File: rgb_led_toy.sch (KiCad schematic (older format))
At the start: 53 parts, among them IC1 AT168, IC2 MBI5168, IC3 MBI5168, IC4 MBI5168, P1 I2C, P2 PORTC, P3 FTDI

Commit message: Moved 'led0' to a hardware PWM pin that is actually free to use.
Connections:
- net led0: now also IC1.10 (PD6(AIN0)); no longer IC1.13 (PB1(OC1A))
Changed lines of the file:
@@
-EESchema Schematic File Version 2  date Tue 10 Jan 2012 11:49:42 AM CET
+EESchema Schematic File Version 2  date Wed 11 Jan 2012 03:03:35 PM CET
 LIBS:power
 LIBS:atmega8_168_328_TQFP
@@
 Sheet 1 1
 Title "RGB LED Toy"
-Date "10 jan 2012"
+Date "11 jan 2012"
 Rev "2.0.d"
 Comp "2012 - My 2muF - blog.spitzenpfeil.org"
@@
 Comment4 ""
 $EndDescr
+NoConn ~ 3950 2100
 NoConn ~ 1550 2200
-Wire Wire Line
-	3950 2100 4050 2100
 Connection ~ 3750 5400
 Connection ~ 3350 5400
@@
 Connection ~ 3950 5400
 NoConn ~ 1550 2700
-NoConn ~ 1550 2600
 NoConn ~ 1550 2500
 NoConn ~ 1550 2400
@@
 	1    0    0    -1
 $EndComp
-Text Label 4050 2100 0    60   ~ 0
+Text Label 1550 2600 2    60   ~ 0
 led0
 Text Label 1800 5300 2    60   ~ 0

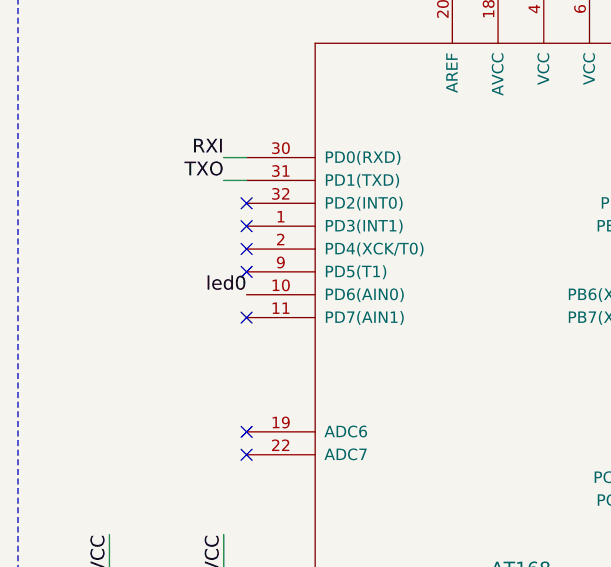
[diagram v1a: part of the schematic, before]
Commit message: Miniscule visual tweak to the schematic.
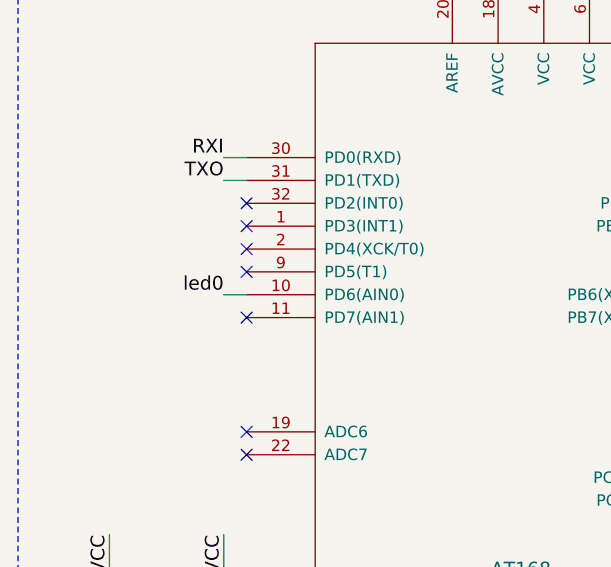
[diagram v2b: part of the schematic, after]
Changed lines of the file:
@@
-EESchema Schematic File Version 2  date Wed 11 Jan 2012 03:03:35 PM CET
+EESchema Schematic File Version 2  date Sat 14 Jan 2012 07:17:03 PM CET
 LIBS:power
 LIBS:atmega8_168_328_TQFP
@@
 Sheet 1 1
 Title "RGB LED Toy"
-Date "11 jan 2012"
+Date "14 jan 2012"
 Rev "2.0.d"
 Comp "2012 - My 2muF - blog.spitzenpfeil.org"
@@
 Comment4 ""
 $EndDescr
-NoConn ~ 3950 2100
-NoConn ~ 1550 2200
 Connection ~ 3750 5400
 Connection ~ 3350 5400
@@
 	2750 5400 4150 5400
 Connection ~ 3950 5400
+Wire Wire Line
+	1450 2600 1550 2600
+NoConn ~ 3950 2100
+NoConn ~ 1550 2200
 NoConn ~ 1550 2700
 NoConn ~ 1550 2500
@@
 	1    0    0    -1
 $EndComp
-Text Label 1550 2600 2    60   ~ 0
+Text Label 1450 2600 2    60   ~ 0
 led0
 Text Label 1800 5300 2    60   ~ 0

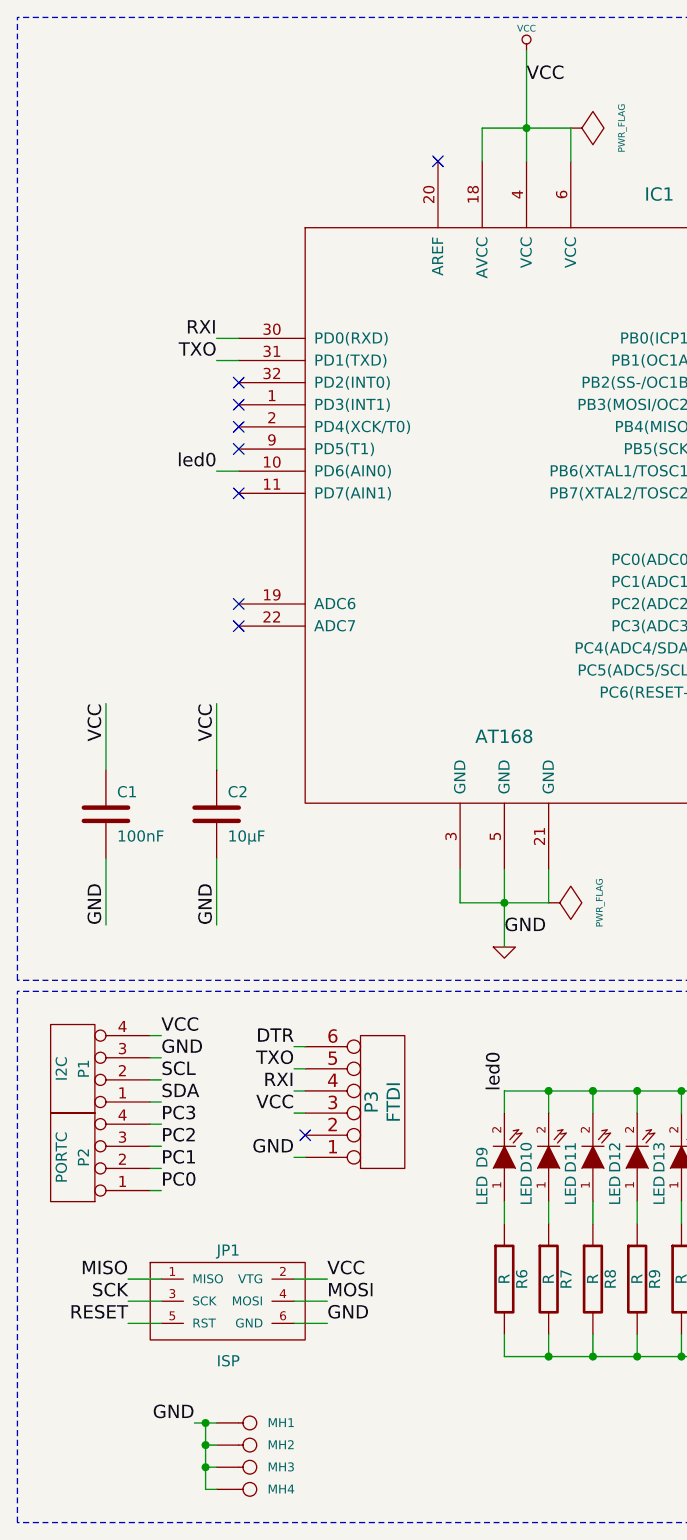
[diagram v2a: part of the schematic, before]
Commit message: Added the TSOP38238 for IR reception to INT0 + some silkscreen art.
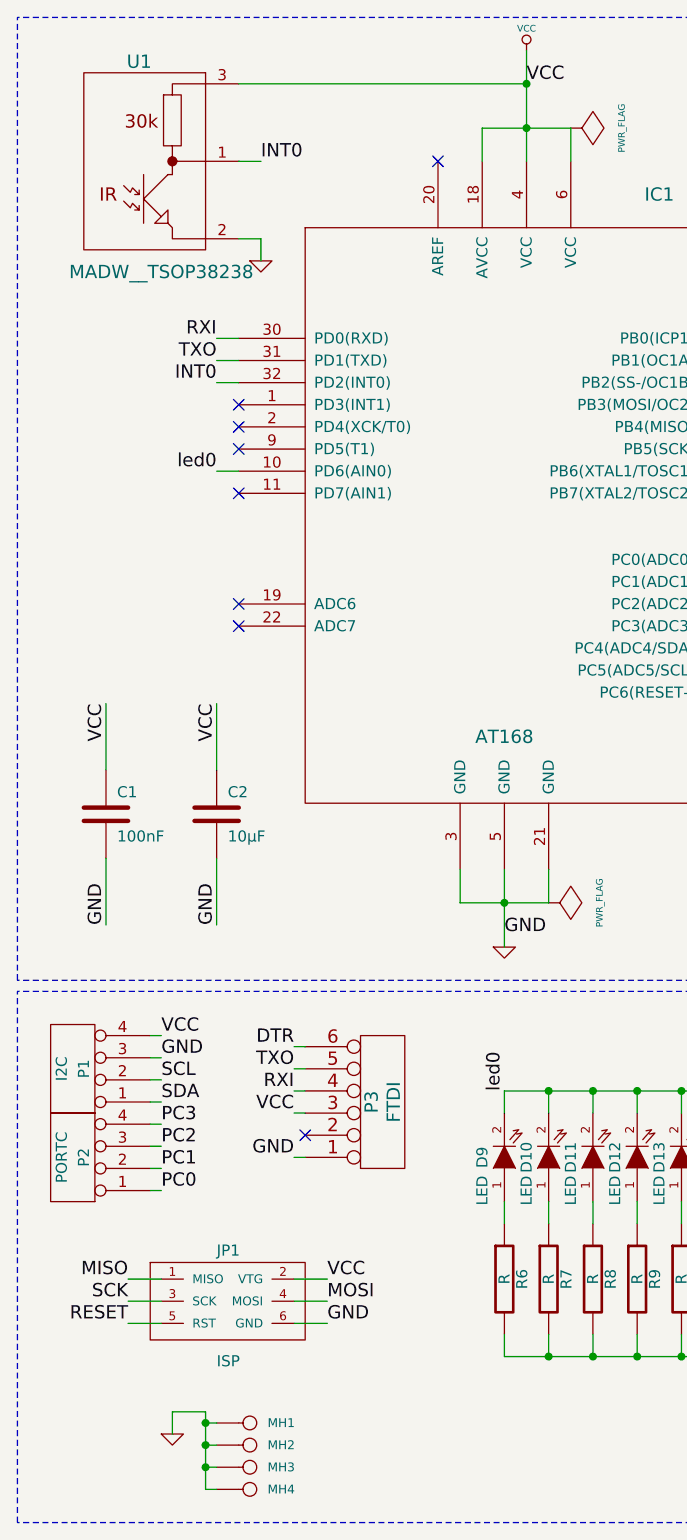
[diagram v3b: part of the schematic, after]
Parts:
- added U1: MADW__TSOP38238, symbol MADW__TSOP38238
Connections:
- net GND: now also U1.2
- net VCC: now also U1.3
- net INT0: now reaches IC1.32 (PD2(INT0))
- net INT0: now also U1.1
- no-connect marks 13 -> 12
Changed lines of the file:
@@
-EESchema Schematic File Version 2  date Sat 14 Jan 2012 07:17:03 PM CET
+EESchema Schematic File Version 2  date Tue 08 May 2012 05:44:56 PM CEST
 LIBS:power
 LIBS:atmega8_168_328_TQFP
@@
 Sheet 1 1
 Title "RGB LED Toy"
-Date "14 jan 2012"
-Rev "2.0.d"
+Date "8 may 2012"
+Rev "2.0.e"
 Comp "2012 - My 2muF - blog.spitzenpfeil.org"
 Comment1 ""
@@
 Comment4 ""
 $EndDescr
+Connection ~ 1400 6900
+Wire Wire Line
+	1250 6950 1250 6850
+Wire Wire Line
+	1250 6850 1400 6850
+Wire Wire Line
+	1400 6850 1400 7200
+Connection ~ 1400 7000
+Wire Wire Line
+	1450 7000 1400 7000
+Wire Wire Line
+	1450 2200 1550 2200
+Connection ~ 2850 850
+Wire Wire Line
+	1550 850  2850 850
 Connection ~ 3750 5400
 Connection ~ 3350 5400
@@
 	1150 5150 1200 5150
 Wire Wire Line
-	1400 7000 1450 7000
-Wire Wire Line
-	1450 7200 1400 7200
-Connection ~ 1400 7000
-Wire Wire Line
 	7250 6550 7300 6550
 Wire Wire Line
@@
 Wire Wire Line
 	6150 6550 6200 6550
-Wire Wire Line
-	1400 7200 1400 6900
-Connection ~ 1400 7100
-Wire Wire Line
-	1400 7100 1450 7100
-Wire Wire Line
-	1450 6900 1350 6900
-Connection ~ 1400 6900
 Wire Wire Line
 	1200 5250 1150 5250
@@
 Wire Wire Line
 	1450 2600 1550 2600
+Wire Wire Line
+	1550 1550 1650 1550
+Wire Wire Line
+	1650 1550 1650 1650
+Wire Wire Line
+	1550 1200 1650 1200
+Wire Wire Line
+	1400 7200 1450 7200
+Wire Wire Line
+	1400 6900 1450 6900
+Wire Wire Line
+	1450 7100 1400 7100
+Connection ~ 1400 7100
+$Comp
+L GND #PWR01
+U 1 1 4FA93F65
+P 1250 6950
+F 0 "#PWR01" H 1250 6950 30  0001 C CNN
+F 1 "GND" H 1250 6880 30  0001 C CNN
+	1    1250 6950
+	1    0    0    -1
+$EndComp
+Text Label 1450 2200 2    60   ~ 0
+INT0
+Text Label 1650 1200 0    60   ~ 0
+INT0
+$Comp
+L GND #PWR02
+U 1 1 4FA92301
+P 1650 1650
+F 0 "#PWR02" H 1650 1650 30  0001 C CNN
+F 1 "GND" H 1650 1580 30  0001 C CNN
+	1    1650 1650
+	1    0    0    -1
+$EndComp
+$Comp
+L MADW__TSOP38238 U1
+U 1 1 4FA922E7
+P 1150 1200
+F 0 "U1" H 1100 1650 60  0000 C CNN
+F 1 "MADW__TSOP38238" H 1200 700 60  0000 C CNN
+	1    1150 1200
+	1    0    0    -1
+$EndComp
 NoConn ~ 3950 2100
-NoConn ~ 1550 2200
 NoConn ~ 1550 2700
 NoConn ~ 1550 2500
@@
 Text Label 6450 4600 2    60   ~ 0
 GND
-Text Label 1350 6900 2    60   ~ 0
-GND
 $Comp
 L CONN_1 MH4
@@
 $EndComp
 $Comp
-L PWR_FLAG #FLG01
+L PWR_FLAG #FLG03
 U 1 1 4EEF9904
 P 2950 4550
-F 0 "#FLG01" H 2950 4820 30  0001 C CNN
+F 0 "#FLG03" H 2950 4820 30  0001 C CNN
 F 1 "PWR_FLAG" H 2950 4780 30  0000 C CNN
 	1    2950 4550
@@
 $EndComp
 $Comp
-L PWR_FLAG #FLG02
+L PWR_FLAG #FLG04
 U 1 1 4EEF98EB
 P 3050 1050
-F 0 "#FLG02" H 3050 1320 30  0001 C CNN
+F 0 "#FLG04" H 3050 1320 30  0001 C CNN
 F 1 "PWR_FLAG" H 3050 1280 30  0000 C CNN
 	1    3050 1050
@@
 GND
 $Comp
-L GND #PWR03
+L GND #PWR05
 U 1 1 49EB3A7A
 P 2750 4750
-F 0 "#PWR03" H 2750 4750 30  0001 C CNN
+F 0 "#PWR05" H 2750 4750 30  0001 C CNN
 F 1 "GND" H 2750 4680 30  0001 C CNN
 	1    2750 4750
@@
 VCC
 $Comp
-L VCC #PWR04
+L VCC #PWR06
 U 1 1 49EB3A61
 P 2850 700
-F 0 "#PWR04" H 2850 800 30  0001 C CNN
+F 0 "#PWR06" H 2850 800 30  0001 C CNN
 F 1 "VCC" H 2850 800 30  0000 C CNN
 	1    2850 700
